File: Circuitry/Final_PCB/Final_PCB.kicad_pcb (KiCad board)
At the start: 2 copper layers, 182.6 x 75.3 mm, 88 parts, among them Q1 Q_NMOS_GDS, Q10 Q_NMOS_GDS, Q11 Q_NMOS_GDS, Q12 Q_NMOS_GDS, Q13 Q_NMOS_GDS, Q14 Q_NMOS_GDS, Q15 Q_NMOS_GDS, Q16 Q_NMOS_GDS, Q2 Q_NMOS_GDS, Q3 Q_NMOS_GDS, Q4 Q_NMOS_GDS, Q5 Q_NMOS_GDS, Q6 Q_NMOS_GDS, Q7 Q_NMOS_GDS, Q8 Q_NMOS_GDS, Q9 Q_NMOS_GDS

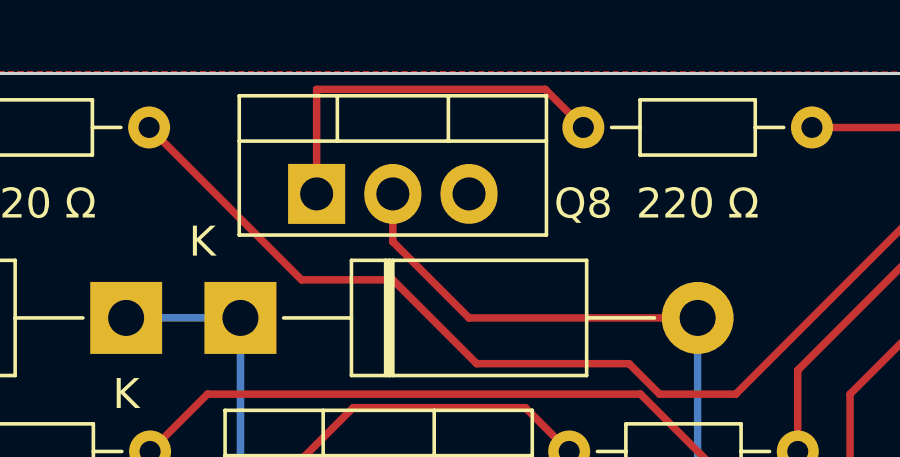
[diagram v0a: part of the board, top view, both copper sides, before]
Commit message: finalize new pcb design, flipped connector location for the LED breakout board
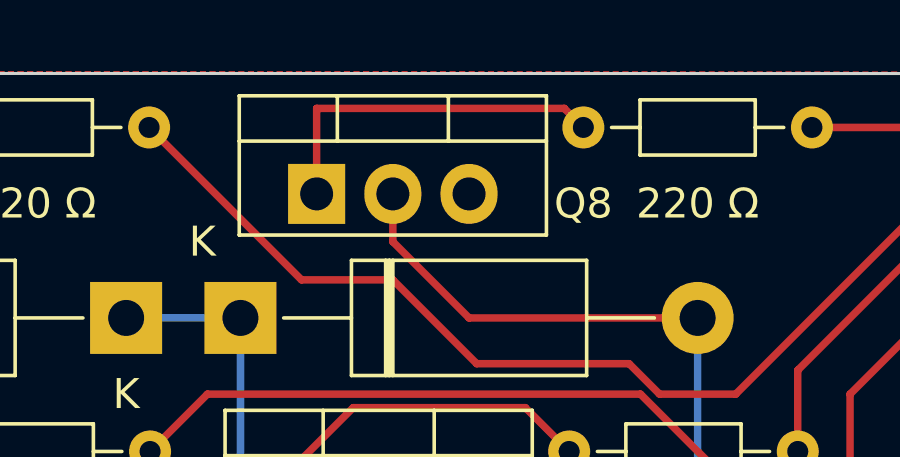
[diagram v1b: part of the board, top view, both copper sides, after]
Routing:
- net Net-(Q8-G): track 12.9 -> 12.0 mm
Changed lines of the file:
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@@
   (segment (start 88.395 70.1025) (end 89.9175 68.58) (width 0.25) (layer "F.Cu") (net 68))
   (segment (start 89.9175 68.58) (end 97.285 68.58) (width 0.25) (layer "F.Cu") (net 68))
-  (segment (start 118.11 67.31) (end 119.38 68.58) (width 0.25) (layer "F.Cu") (net 69))
-  (segment (start 110.49 67.31) (end 118.11 67.31) (width 0.25) (layer "F.Cu") (net 69))
-  (segment (start 110.49 70.795) (end 110.49 67.31) (width 0.25) (layer "F.Cu") (net 69))
+  (segment (start 110.49 67.945) (end 118.745 67.945) (width 0.25) (layer "F.Cu") (net 69))
+  (segment (start 118.745 67.945) (end 119.38 68.58) (width 0.25) (layer "F.Cu") (net 69))
+  (segment (start 110.49 70.795) (end 110.49 67.945) (width 0.25) (layer "F.Cu") (net 69))
   (segment (start 140.61 101.6) (end 147.32 101.6) (width 0.25) (layer "F.Cu") (net 70))
   (segment (start 138.395 103.815) (end 140.61 101.6) (width 0.25) (layer "F.Cu") (net 70))
